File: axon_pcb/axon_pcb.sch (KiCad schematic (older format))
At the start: 100 parts, among them J1 USB_C_Receptacle, J2 AVR_ISP Header, K1 KEYSW, K10 KEYSW, K11 KEYSW, K12 KEYSW, K13 KEYSW, K14 KEYSW, K15 KEYSW, K16 KEYSW, K17 KEYSW, K18 KEYSW, K19 KEYSW, K2 KEYSW, K20 KEYSW, K21 KEYSW, K22 KEYSW, K23 KEYSW, K24 KEYSW, K25 KEYSW, K26 KEYSW, K27 KEYSW, K28 KEYSW, K29 KEYSW, K3 KEYSW, K30 KEYSW, K31 KEYSW, K32 KEYSW, K33 KEYSW, K34 KEYSW, K35 KEYSW, K36 KEYSW, K37 KEYSW, K38 KEYSW, K39 KEYSW, K4 KEYSW, K40 KEYSW, K5 KEYSW, K6 KEYSW, K7 KEYSW, K8 KEYSW, K9 KEYSW, SW1 RESET, SW2 BOOT, U1 ATmega328P-PU, X1 16MHz

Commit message: tweaked component placements: - components further from edges - less difference in USB data line lengths (now less than 2 mm) - made crystal cap trace lengths more samey
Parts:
- J2: footprint Connector_PinHeader_2.54mm:PinHeader_2x03_P2.54mm_Vertical -> personal:PinHeader_2x03_P2.54mm_Vertical
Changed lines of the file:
@@
 F 0 "J2" H 8050 5467 50  0000 C CNN
 F 1 "AVR_ISP Header" H 8050 5376 50  0000 C CNN
-F 2 "Connector_PinHeader_2.54mm:PinHeader_2x03_P2.54mm_Vertical" H 8000 5150 50  0001 C CNN
+F 2 "personal:PinHeader_2x03_P2.54mm_Vertical" H 8000 5150 50  0001 C CNN
 F 3 "~" H 8000 5150 50  0001 C CNN
 	1    8000 5150

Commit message: fixed libraries, final pcb version
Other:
- moved on the sheet: C1, C2, R1, SW1, SW2, U1, X1

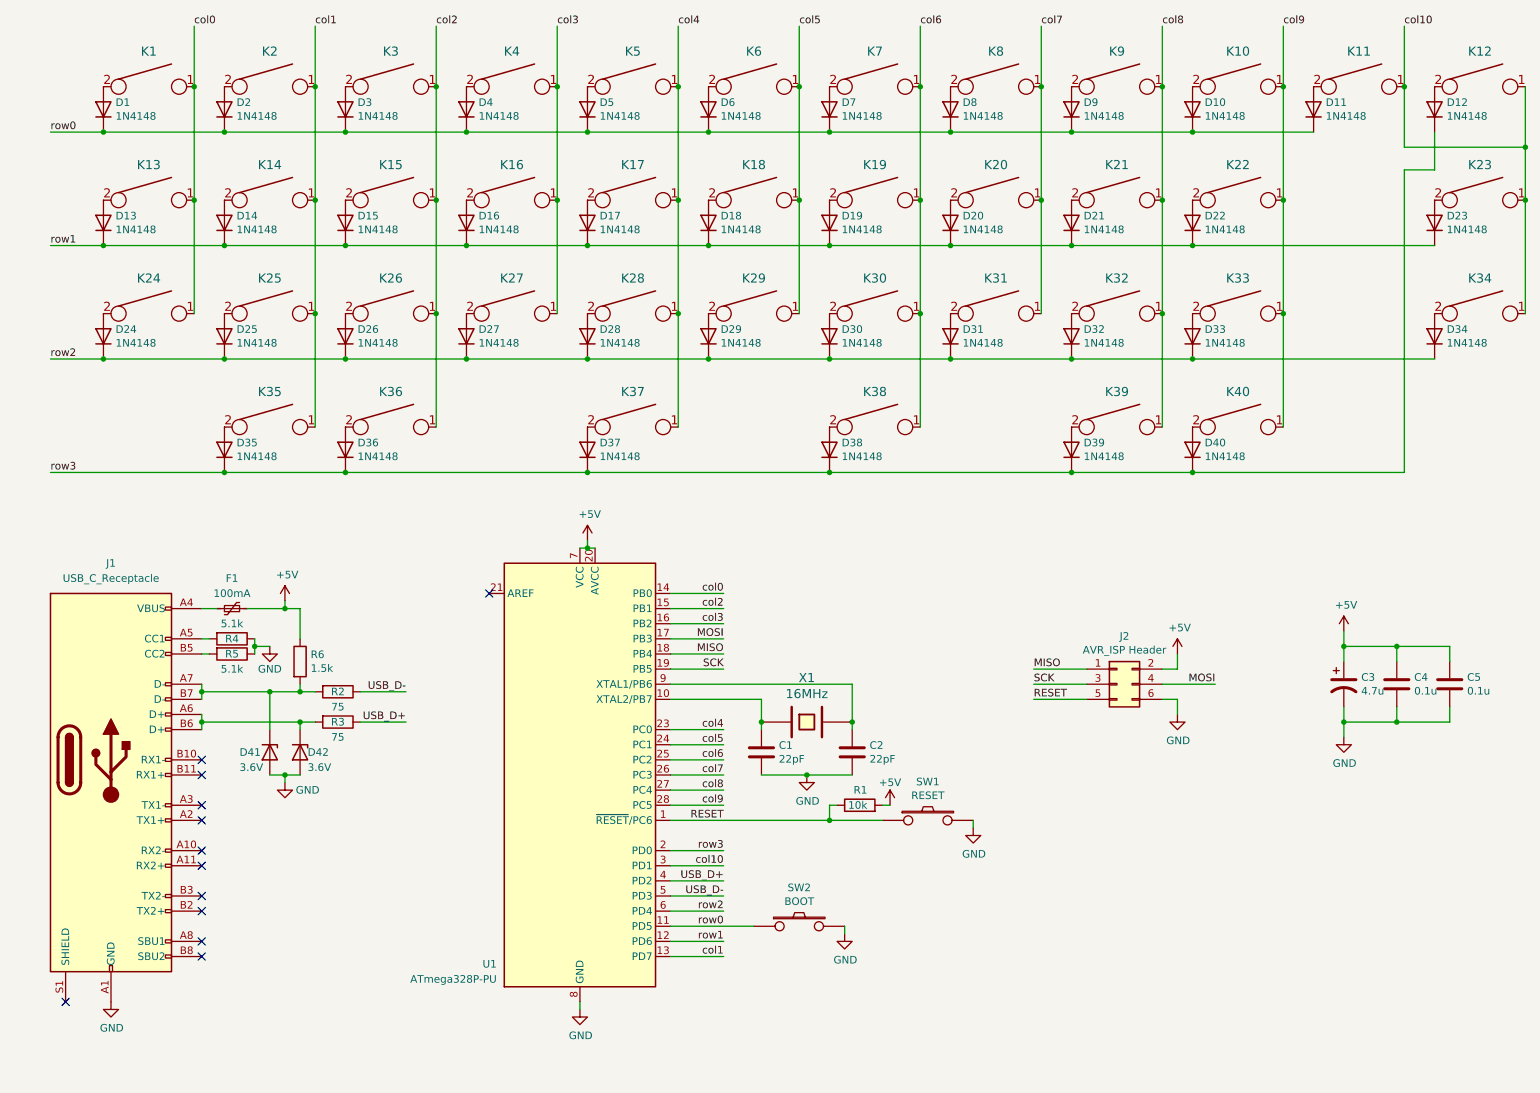
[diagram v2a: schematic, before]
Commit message: rerouting and added alt spacebar config
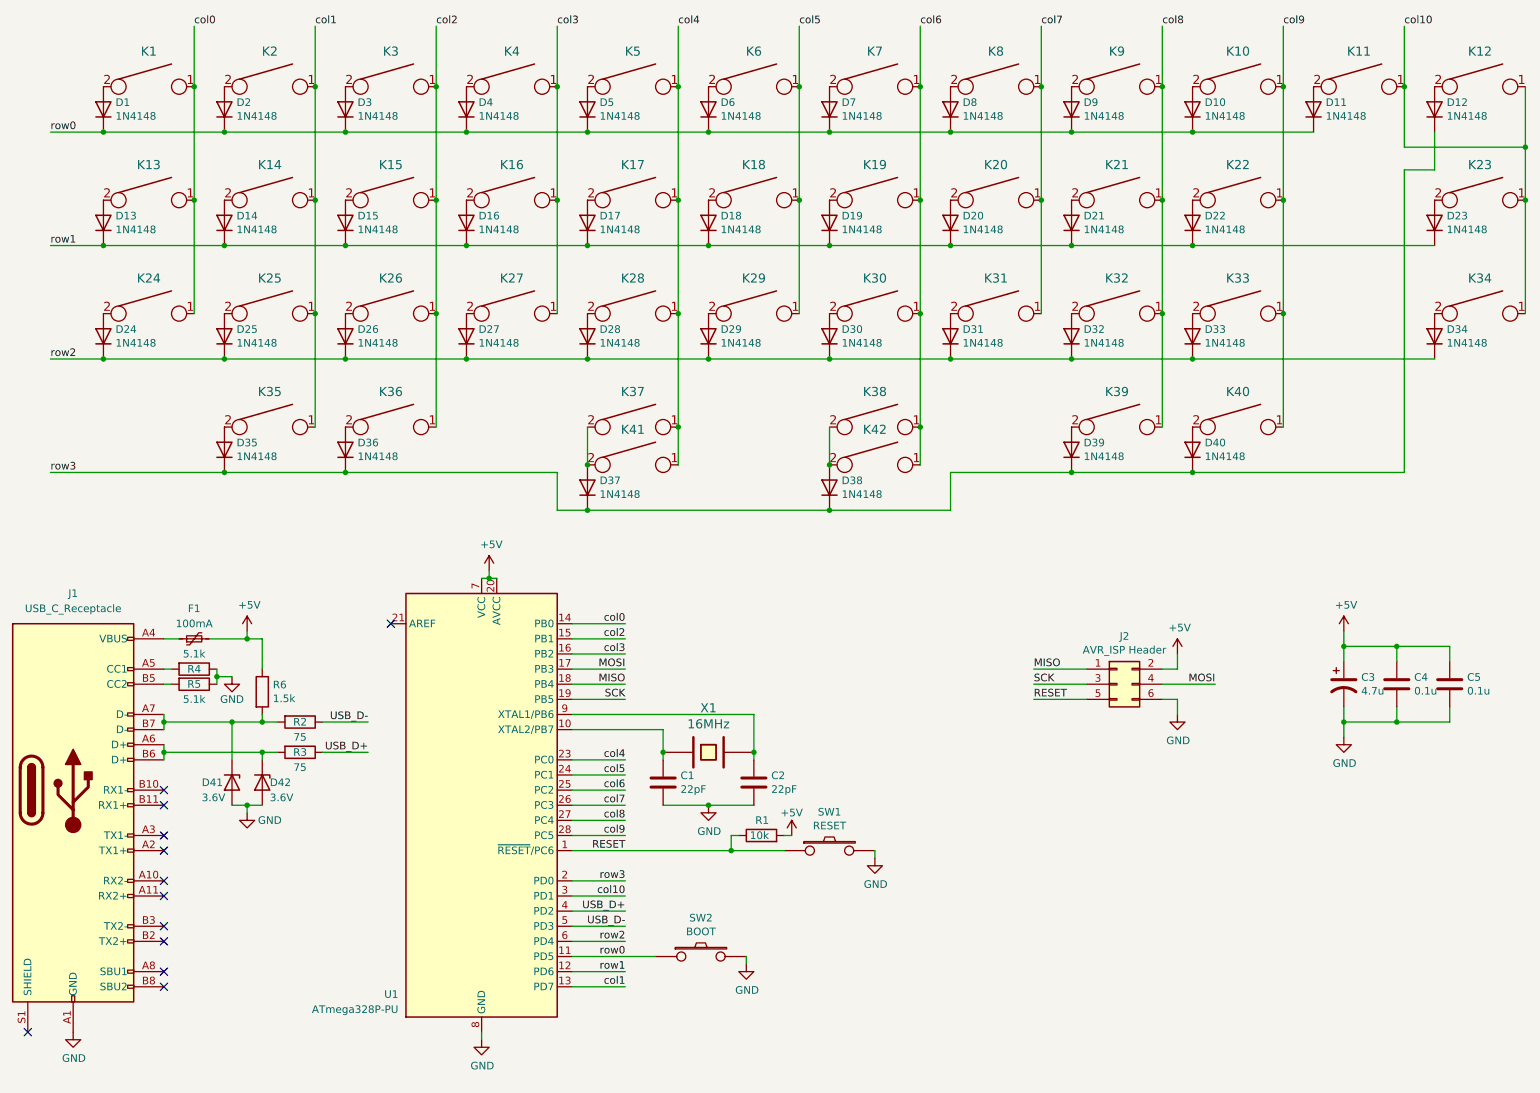
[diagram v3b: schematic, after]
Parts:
- added K41, K42: KEYSW, keyswitches-daprice:SW_MX, symbol keyboard-parts:KEYSW
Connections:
- net col4: now also K41.1
- net col6: now also K42.1
- net at D37.2 (A), K37.2: now also K41.2
- net at D38.2 (A), K38.2: now also K42.2
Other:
- moved on the sheet: C1, C2, D37, D38, D41, D42, F1, J1, R1, R2, R3, R4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

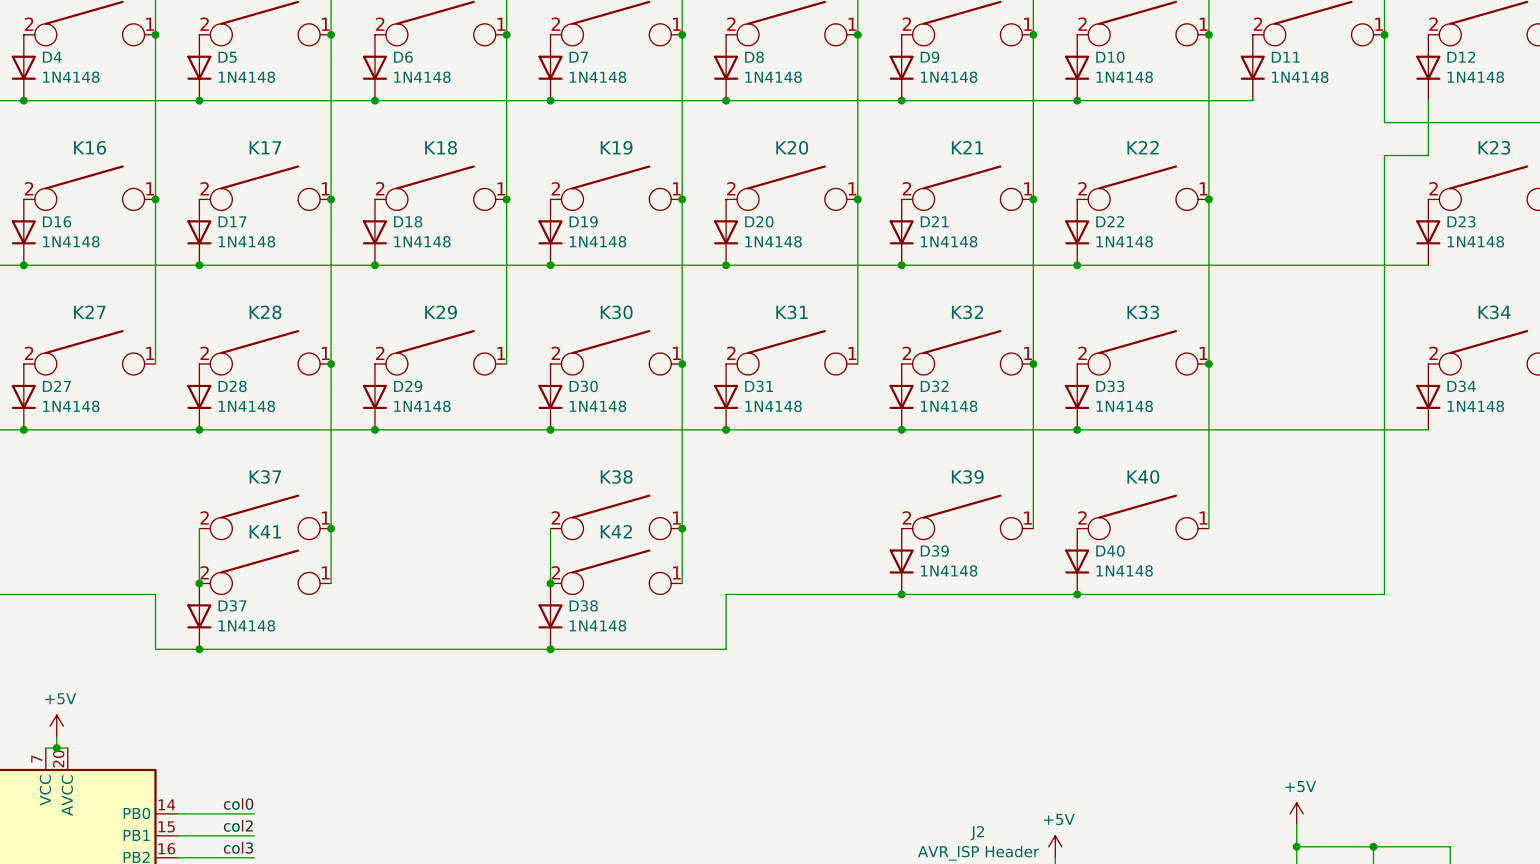
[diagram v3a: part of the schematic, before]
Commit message: added 7u support
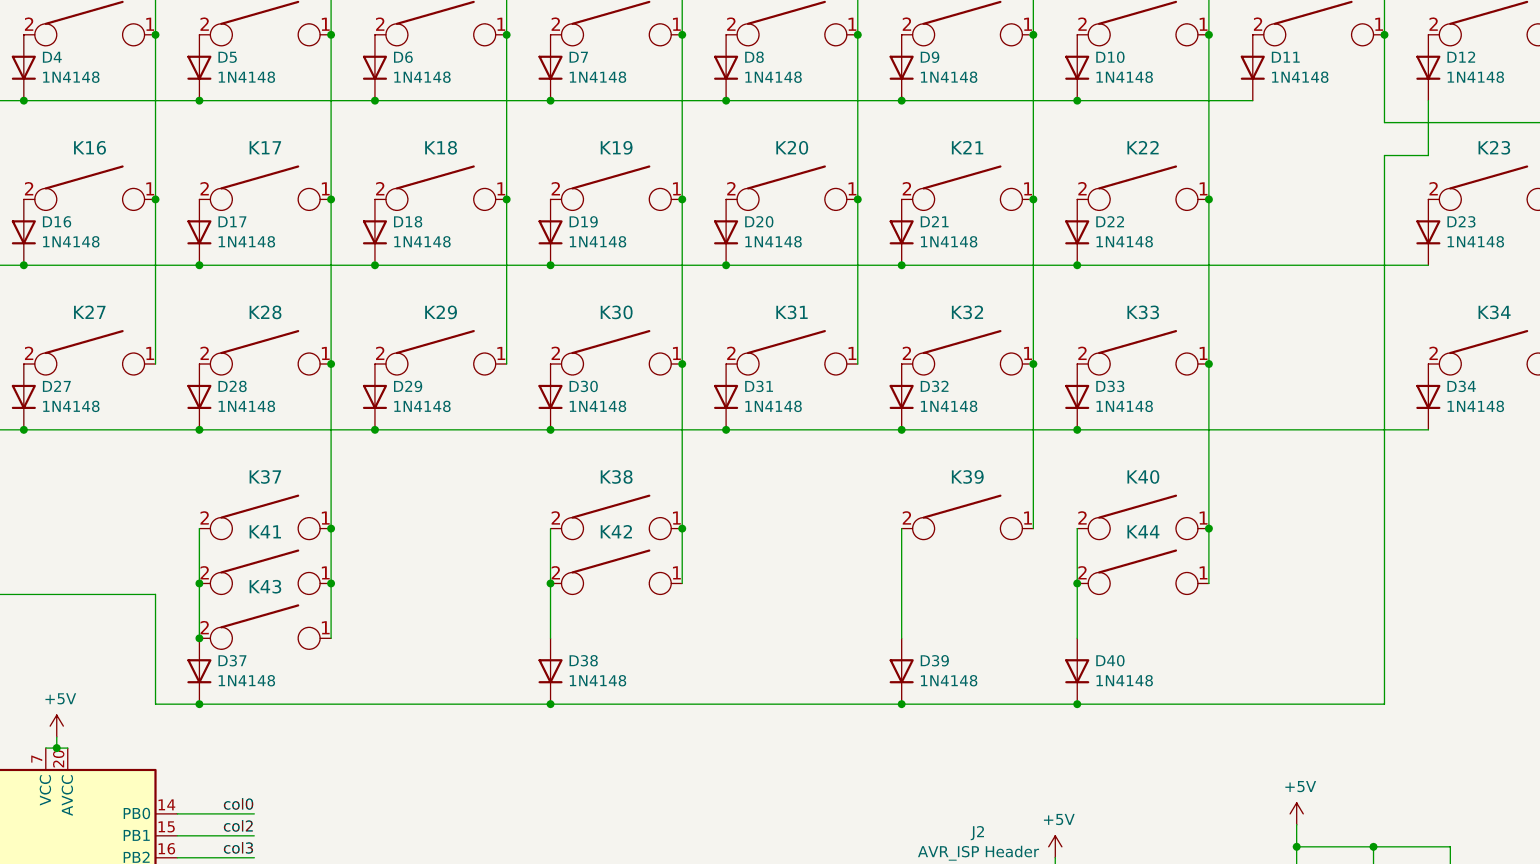
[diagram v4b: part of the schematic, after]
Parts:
- added K43, K44: KEYSW, keyswitches-daprice:SW_MX, symbol keyboard-parts:KEYSW
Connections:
- net col4: now also K43.1
- net col9: now also K44.1
- net at D37.2 (A), K37.2, K41.2: now also K43.2
- net at D40.2 (A), K40.2: now also K44.2
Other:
- moved on the sheet: D37, D38, D39, D40
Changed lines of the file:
@@
-$EndComp
-$Comp
-L keyboard-parts:KEYSW K37
-U 1 1 6058034D
-P 4800 3450
-F 0 "K37" H 4800 3683 60  0000 C CNN
-F 1 "KEYSW" H 4800 3350 60  0001 C CNN
-F 2 "keyswitches-daprice:SW_MX" H 4800 3450 60  0001 C CNN
-F 3 "" H 4800 3450 60  0000 C CNN
-	1    4800 3450
-	1    0    0    -1
 $EndComp
 $Comp
@@
 Wire Wire Line
 	10700 1950 10700 2700
-Wire Wire Line
-	9900 3750 9900 1750
 Wire Wire Line
 	9900 1750 10100 1750
@@
 L Diode:1N4148 D40
 U 1 1 60633498
-P 8500 3600
-F 0 "D40" V 8546 3520 50  0000 R CNN
-F 1 "1N4148" V 8455 3520 50  0000 R CNN
-F 2 "Diode_THT:D_DO-35_SOD27_P7.62mm_Horizontal" H 8500 3425 50  0001 C CNN
-F 3 "https://assets.nexperia.com/documents/data-sheet/1N4148_1N4448.pdf" H 8500 3600 50  0001 C CNN
-	1    8500 3600
-	0    -1   -1   0
-$EndComp
-Connection ~ 8500 3750
-Wire Wire Line
-	8500 3750 9900 3750
+P 8500 4100
+F 0 "D40" V 8546 4020 50  0000 R CNN
+F 1 "1N4148" V 8455 4020 50  0000 R CNN
+F 2 "Diode_THT:D_DO-35_SOD27_P7.62mm_Horizontal" H 8500 3925 50  0001 C CNN
+F 3 "https://assets.nexperia.com/documents/data-sheet/1N4148_1N4448.pdf" H 8500 4100 50  0001 C CNN
+	1    8500 4100
+	0    -1   -1   0
+$EndComp
 $Comp
 L Diode:1N4148 D39
 U 1 1 60633D78
-P 7700 3600
-F 0 "D39" V 7746 3520 50  0000 R CNN
-F 1 "1N4148" V 7655 3520 50  0000 R CNN
-F 2 "Diode_THT:D_DO-35_SOD27_P7.62mm_Horizontal" H 7700 3425 50  0001 C CNN
-F 3 "https://assets.nexperia.com/documents/data-sheet/1N4148_1N4448.pdf" H 7700 3600 50  0001 C CNN
-	1    7700 3600
-	0    -1   -1   0
-$EndComp
-Wire Wire Line
-	7700 3750 8500 3750
+P 7700 4100
+F 0 "D39" V 7746 4020 50  0000 R CNN
+F 1 "1N4148" V 7655 4020 50  0000 R CNN
+F 2 "Diode_THT:D_DO-35_SOD27_P7.62mm_Horizontal" H 7700 3925 50  0001 C CNN
+F 3 "https://assets.nexperia.com/documents/data-sheet/1N4148_1N4448.pdf" H 7700 4100 50  0001 C CNN
+	1    7700 4100
+	0    -1   -1   0
+$EndComp
 $Comp
 L Diode:1N4148 D38
 U 1 1 606345E8
-P 6100 3850
-F 0 "D38" V 6146 3770 50  0000 R CNN
-F 1 "1N4148" V 6055 3770 50  0000 R CNN
-F 2 "Diode_THT:D_DO-35_SOD27_P7.62mm_Horizontal" H 6100 3675 50  0001 C CNN
-F 3 "https://assets.nexperia.com/documents/data-sheet/1N4148_1N4448.pdf" H 6100 3850 50  0001 C CNN
-	1    6100 3850
+P 6100 4100
+F 0 "D38" V 6146 4020 50  0000 R CNN
+F 1 "1N4148" V 6055 4020 50  0000 R CNN
+F 2 "Diode_THT:D_DO-35_SOD27_P7.62mm_Horizontal" H 6100 3925 50  0001 C CNN
+F 3 "https://assets.nexperia.com/documents/data-sheet/1N4148_1N4448.pdf" H 6100 4100 50  0001 C CNN
+	1    6100 4100
 	0    -1   -1   0
 $EndComp
@@
 L Diode:1N4148 D37
 U 1 1 60634EA0
-P 4500 3850
-F 0 "D37" V 4546 3770 50  0000 R CNN
-F 1 "1N4148" V 4455 3770 50  0000 R CNN
-F 2 "Diode_THT:D_DO-35_SOD27_P7.62mm_Horizontal" H 4500 3675 50  0001 C CNN
-F 3 "https://assets.nexperia.com/documents/data-sheet/1N4148_1N4448.pdf" H 4500 3850 50  0001 C CNN
-	1    4500 3850
+P 4500 4100
+F 0 "D37" V 4546 4020 50  0000 R CNN
+F 1 "1N4148" V 4455 4020 50  0000 R CNN
+F 2 "Diode_THT:D_DO-35_SOD27_P7.62mm_Horizontal" H 4500 3925 50  0001 C CNN
+F 3 "https://assets.nexperia.com/documents/data-sheet/1N4148_1N4448.pdf" H 4500 4100 50  0001 C CNN
+	1    4500 4100
 	0    -1   -1   0
 $EndComp
@@
 Wire Wire Line
 	4500 3450 4500 3700
-Connection ~ 4500 3700
 Wire Wire Line
 	5100 3450 5100 3700
 Connection ~ 5100 3450
-Wire Wire Line
-	4300 3750 4300 4000
-Wire Wire Line
-	4300 4000 4500 4000
+$Comp
+L keyboard-parts:KEYSW K37
+U 1 1 6058034D
+P 4800 3450
+F 0 "K37" H 4800 3683 60  0000 C CNN
+F 1 "KEYSW" H 4800 3350 60  0001 C CNN
+F 2 "keyswitches-daprice:SW_MX" H 4800 3450 60  0001 C CNN
+F 3 "" H 4800 3450 60  0000 C CNN
+	1    4800 3450
+	1    0    0    -1
+$EndComp
+$Comp
+L keyboard-parts:KEYSW K43
+U 1 1 60968780
+P 4800 3950
+F 0 "K43" H 4800 4183 60  0000 C CNN
+F 1 "KEYSW" H 4800 3850 60  0001 C CNN
+F 2 "keyswitches-daprice:SW_MX" H 4800 3950 60  0001 C CNN
+F 3 "" H 4800 3950 60  0000 C CNN
+	1    4800 3950
+	1    0    0    -1
+$EndComp
+Wire Wire Line
+	6100 3700 6100 3950
 Connection ~ 6100 3700
 Wire Wire Line
-	6900 4000 6900 3750
-Wire Wire Line
-	6900 3750 7700 3750
-Wire Wire Line
-	4500 4000 6100 4000
-Connection ~ 4500 4000
-Connection ~ 6100 4000
-Wire Wire Line
-	6100 4000 6900 4000
-Connection ~ 7700 3750
+	6100 4250 4500 4250
+Connection ~ 6100 4250
+Wire Wire Line
+	4500 4250 4300 4250
+Wire Wire Line
+	4300 3750 4300 4250
+Connection ~ 4500 4250
+Wire Wire Line
+	4500 3700 4500 3950
+Connection ~ 4500 3700
+Connection ~ 4500 3950
+Wire Wire Line
+	5100 3700 5100 3950
+Connection ~ 5100 3700
+$Comp
+L keyboard-parts:KEYSW K44
+U 1 1 609D318E
+P 8800 3700
+F 0 "K44" H 8800 3933 60  0000 C CNN
+F 1 "KEYSW" H 8800 3600 60  0001 C CNN
+F 2 "keyswitches-daprice:SW_MX" H 8800 3700 60  0001 C CNN
+F 3 "" H 8800 3700 60  0000 C CNN
+	1    8800 3700
+	1    0    0    -1
+$EndComp
+Wire Wire Line
+	9100 3450 9100 3700
+Connection ~ 9100 3450
+Wire Wire Line
+	8500 3450 8500 3700
+Wire Wire Line
+	9900 1750 9900 4250
+Wire Wire Line
+	6100 4250 7700 4250
+Connection ~ 8500 4250
+Wire Wire Line
+	8500 4250 9900 4250
+Connection ~ 7700 4250
+Wire Wire Line
+	7700 4250 8500 4250
+Wire Wire Line
+	7700 3450 7700 3950
+Wire Wire Line
+	8500 3700 8500 3950
+Connection ~ 8500 3700
 $EndSCHEMATC
